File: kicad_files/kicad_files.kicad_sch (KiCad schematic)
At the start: 0 parts

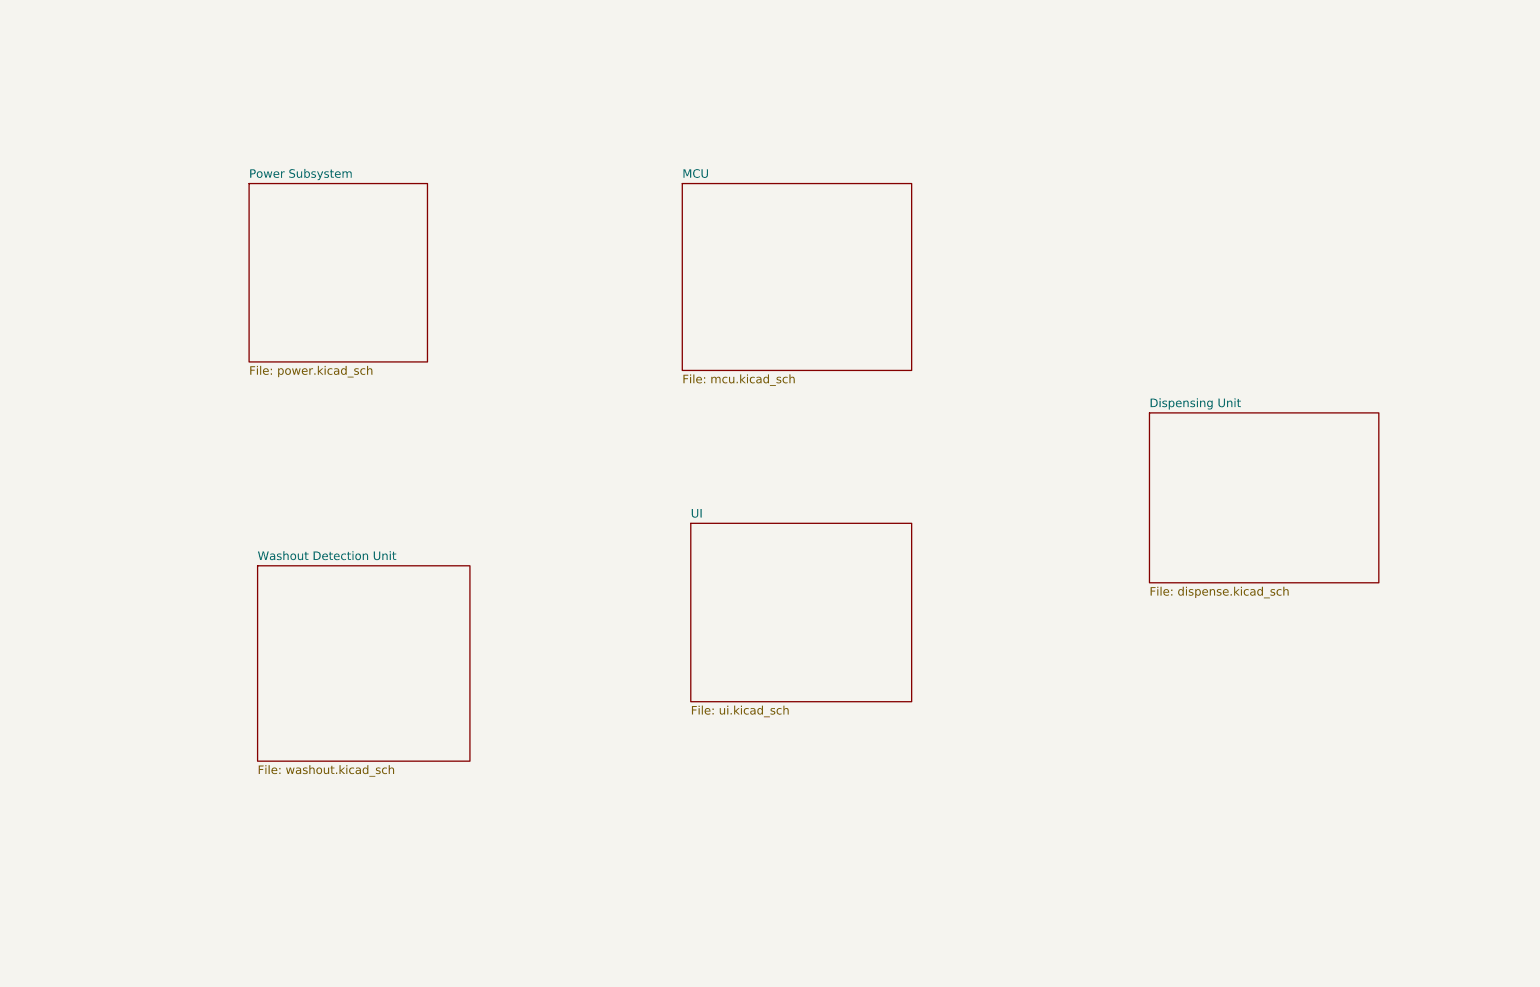
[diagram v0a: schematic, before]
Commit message: UI schematic and external connectors
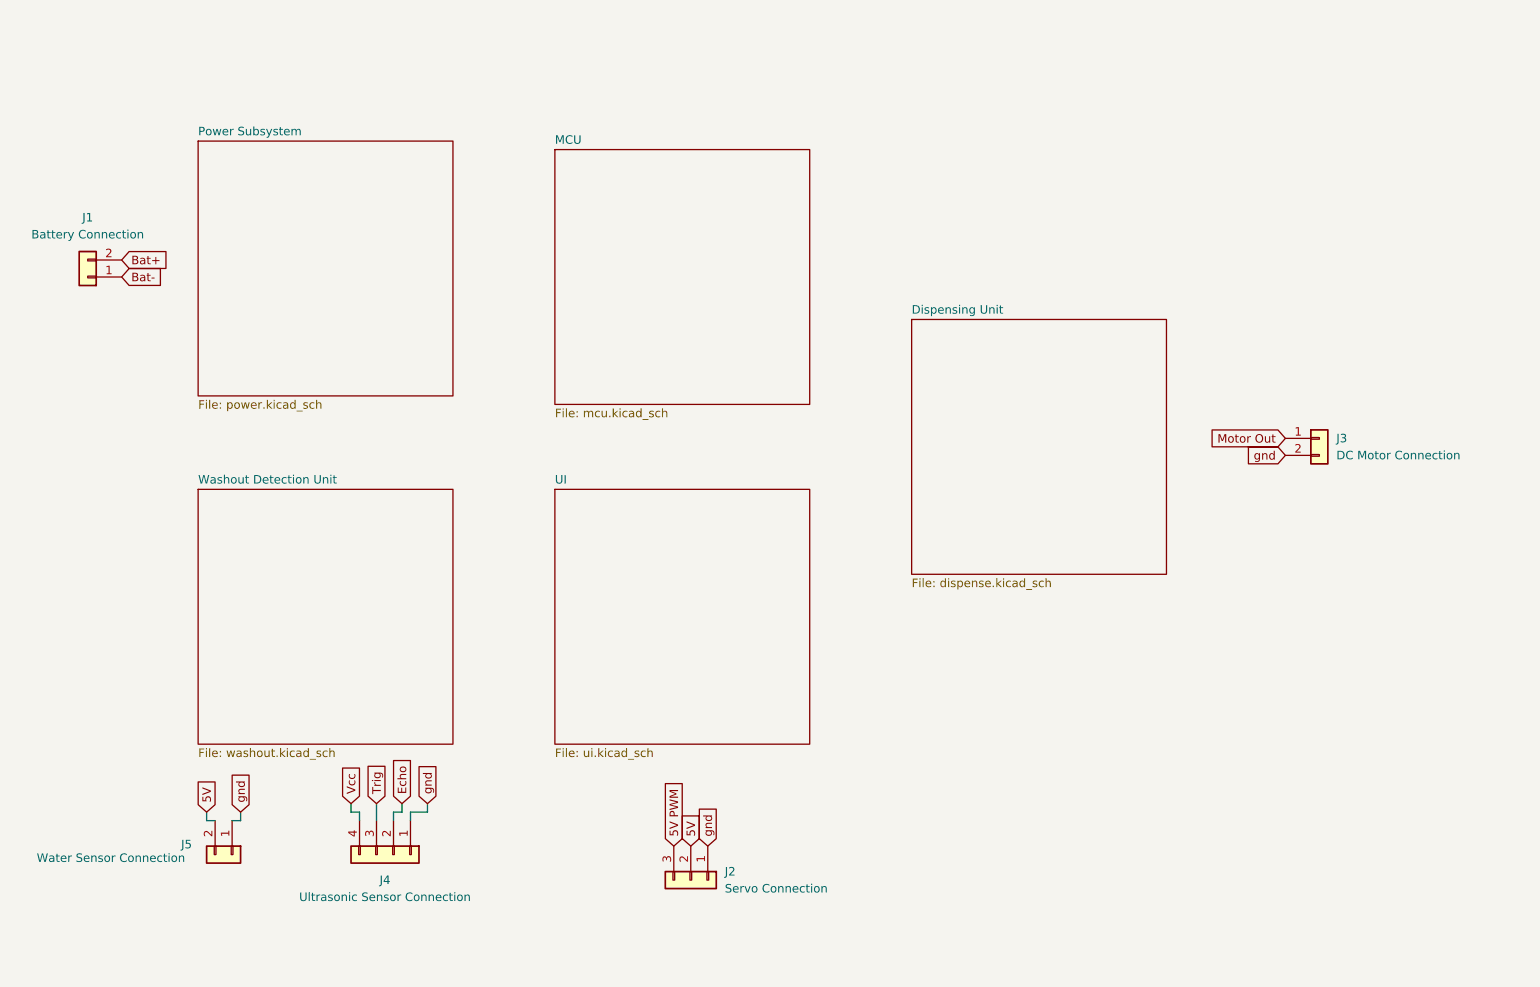
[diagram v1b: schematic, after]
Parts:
- added J1: Battery Connection, symbol Connector_Generic:Conn_01x02
- added J2: Servo Connection, symbol Connector_Generic:Conn_01x03
- added J3: DC Motor Connection, symbol Connector_Generic:Conn_01x02
- added J4: Ultrasonic Sensor Connection, symbol Connector_Generic:Conn_01x04
- added J5: Water Sensor Connection, symbol Connector_Generic:Conn_01x02
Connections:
- new net 5V: J2.2 (Pin_2), J5.2 (Pin_2)
- new net 5V PWM: J2.3 (Pin_3)
- new net Bat+: J1.2 (Pin_2)
- new net Bat-: J1.1 (Pin_1)
- new net Echo: J4.2 (Pin_2)
- new net Motor Out: J3.1 (Pin_1)
- new net Trig: J4.3 (Pin_3)
- new net Vcc: J4.4 (Pin_4)
- new net gnd: J2.1 (Pin_1), J3.2 (Pin_2), J4.1 (Pin_1), J5.1 (Pin_1)

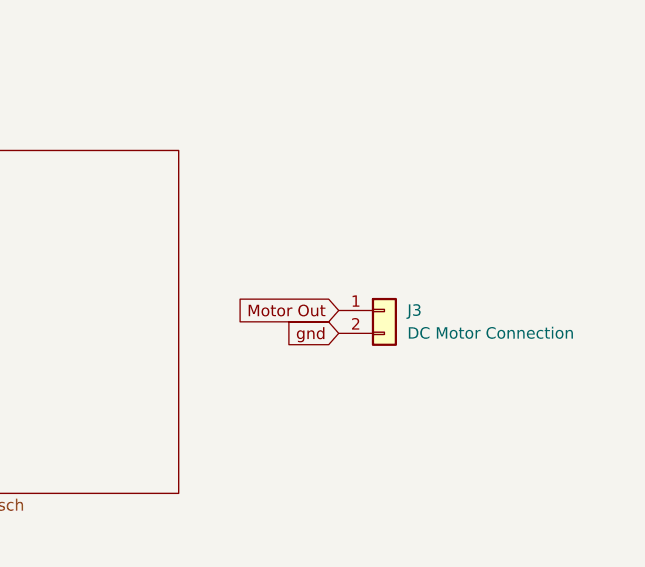
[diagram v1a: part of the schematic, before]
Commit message: UI, washout detection, motor schematics finished
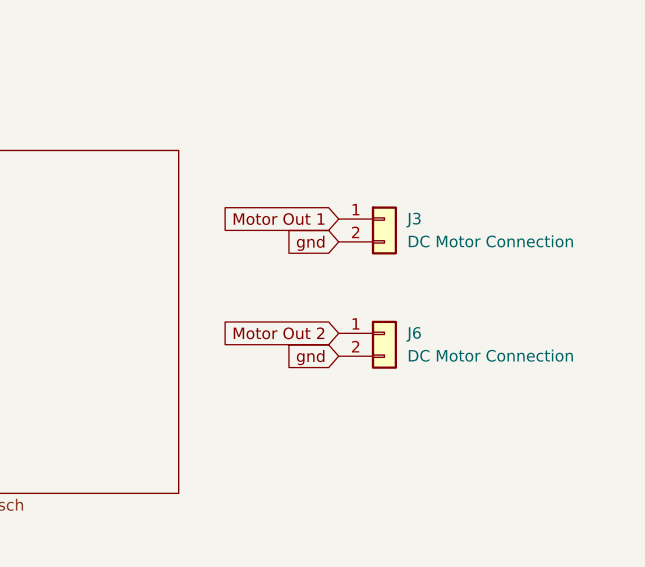
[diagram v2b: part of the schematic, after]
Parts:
- added J6: DC Motor Connection, symbol Connector_Generic:Conn_01x02
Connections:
- net gnd: now also J6.2 (Pin_2)
- net Motor Out renamed Motor Out 1
- new net Motor Out 2: J6.1 (Pin_1)
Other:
- moved on the sheet: J3
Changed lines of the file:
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@@
+		)
+	)
+	(global_label "Motor Out 2"
+		(shape input)
+		(at 207.01 110.49 180)
+		(fields_autoplaced yes)
+		(effects
+			(font
+				(size 1.27 1.27)
+			)
+			(justify right)
+		)
+		(property "Intersheetrefs" "${INTERSHEET_REFS}"
+			(at 192.4136 110.49 0)
+			(effects
+				(font
+					(size 1.27 1.27)
+				)
+				(justify right)
+				(hide yes)
+			)
 		)
 	)
@@
 		)
 	)
+	(global_label "gnd"
+		(shape input)
+		(at 207.01 113.03 180)
+		(fields_autoplaced yes)
+		(effects
+			(font
+				(size 1.27 1.27)
+			)
+			(justify right)
+		)
+		(property "Intersheetrefs" "${INTERSHEET_REFS}"
+			(at 200.5778 113.03 0)
+			(effects
+				(font
+					(size 1.27 1.27)
+				)
+				(justify right)
+				(hide yes)
+			)
+		)
+	)
 	(global_label "Vcc"
 		(shape input)
@@
 		)
 	)
-	(global_label "Motor Out"
-		(shape input)
-		(at 207.01 107.95 180)
+	(global_label "Motor Out 1"
+		(shape input)
+		(at 207.01 97.79 180)
 		(fields_autoplaced yes)
 		(effects
@@
 		)
 		(property "Intersheetrefs" "${INTERSHEET_REFS}"
-			(at 194.5907 107.95 0)
+			(at 192.4136 97.79 0)
 			(effects
 				(font
@@
 	(global_label "gnd"
 		(shape input)
-		(at 207.01 110.49 180)
+		(at 207.01 100.33 180)
 		(fields_autoplaced yes)
 		(effects
@@
 		)
 		(property "Intersheetrefs" "${INTERSHEET_REFS}"
-			(at 200.5778 110.49 0)
+			(at 200.5778 100.33 0)
 			(effects
 				(font
@@
 	(symbol
 		(lib_id "Connector_Generic:Conn_01x02")
-		(at 212.09 107.95 0)
+		(at 212.09 110.49 0)
 		(unit 1)
 		(exclude_from_sim no)
@@
 		(dnp no)
 		(fields_autoplaced yes)
+		(property "Reference" "J6"
+			(at 214.63 110.4899 0)
+			(effects
+				(font
+					(size 1.27 1.27)
+				)
+				(justify left)
+			)
+		)
+		(property "Value" "DC Motor Connection"
+			(at 214.63 113.0299 0)
+			(effects
+				(font
+					(size 1.27 1.27)
+				)
+				(justify left)
+			)
+		)
+		(property "Footprint" ""
+			(at 212.09 110.49 0)
+			(effects
+				(font
+					(size 1.27 1.27)
+				)
+				(hide yes)
+			)
+		)
+		(property "Datasheet" "~"
+			(at 212.09 110.49 0)
+			(effects
+				(font
+					(size 1.27 1.27)
+				)
+				(hide yes)
+			)
+		)
+		(property "Description" "Generic connector, single row, 01x02, script generated (kicad-library-utils/schlib/autogen/connector/)"
+			(at 212.09 110.49 0)
+			(effects
+				(font
+					(size 1.27 1.27)
+				)
+				(hide yes)
+			)
+		)
+		(pin "2"
+		)
+		(pin "1"
+		)
+		(instances
+			(project "kicad_files"
+				(path "/67de3bec-6c8a-4e66-9cf7-9a8a92865209"
+					(reference "J6")
+					(unit 1)
+				)
+			)
+		)
+	)
+	(symbol
+		(lib_id "Connector_Generic:Conn_01x02")
+		(at 212.09 97.79 0)
+		(unit 1)
+		(exclude_from_sim no)
+		(in_bom yes)
+		(on_board yes)
+		(dnp no)
+		(fields_autoplaced yes)
 		(property "Reference" "J3"
-			(at 214.63 107.9499 0)
+			(at 214.63 97.7899 0)
 			(effects
 				(font
@@
 		)
 		(property "Value" "DC Motor Connection"
-			(at 214.63 110.4899 0)
+			(at 214.63 100.3299 0)
 			(effects
 				(font
@@
 		)
 		(property "Footprint" ""
-			(at 212.09 107.95 0)
+			(at 212.09 97.79 0)
 			(effects
 				(font
@@
 		)
 		(property "Datasheet" "~"
-			(at 212.09 107.95 0)
+			(at 212.09 97.79 0)
 			(effects
 				(font
@@
 		)
 		(property "Description" "Generic connector, single row, 01x02, script generated (kicad-library-utils/schlib/autogen/connector/)"
-			(at 212.09 107.95 0)
-			(effects
-				(font
+			(at 212.09 97.79 0)
+			(effects
+				(font

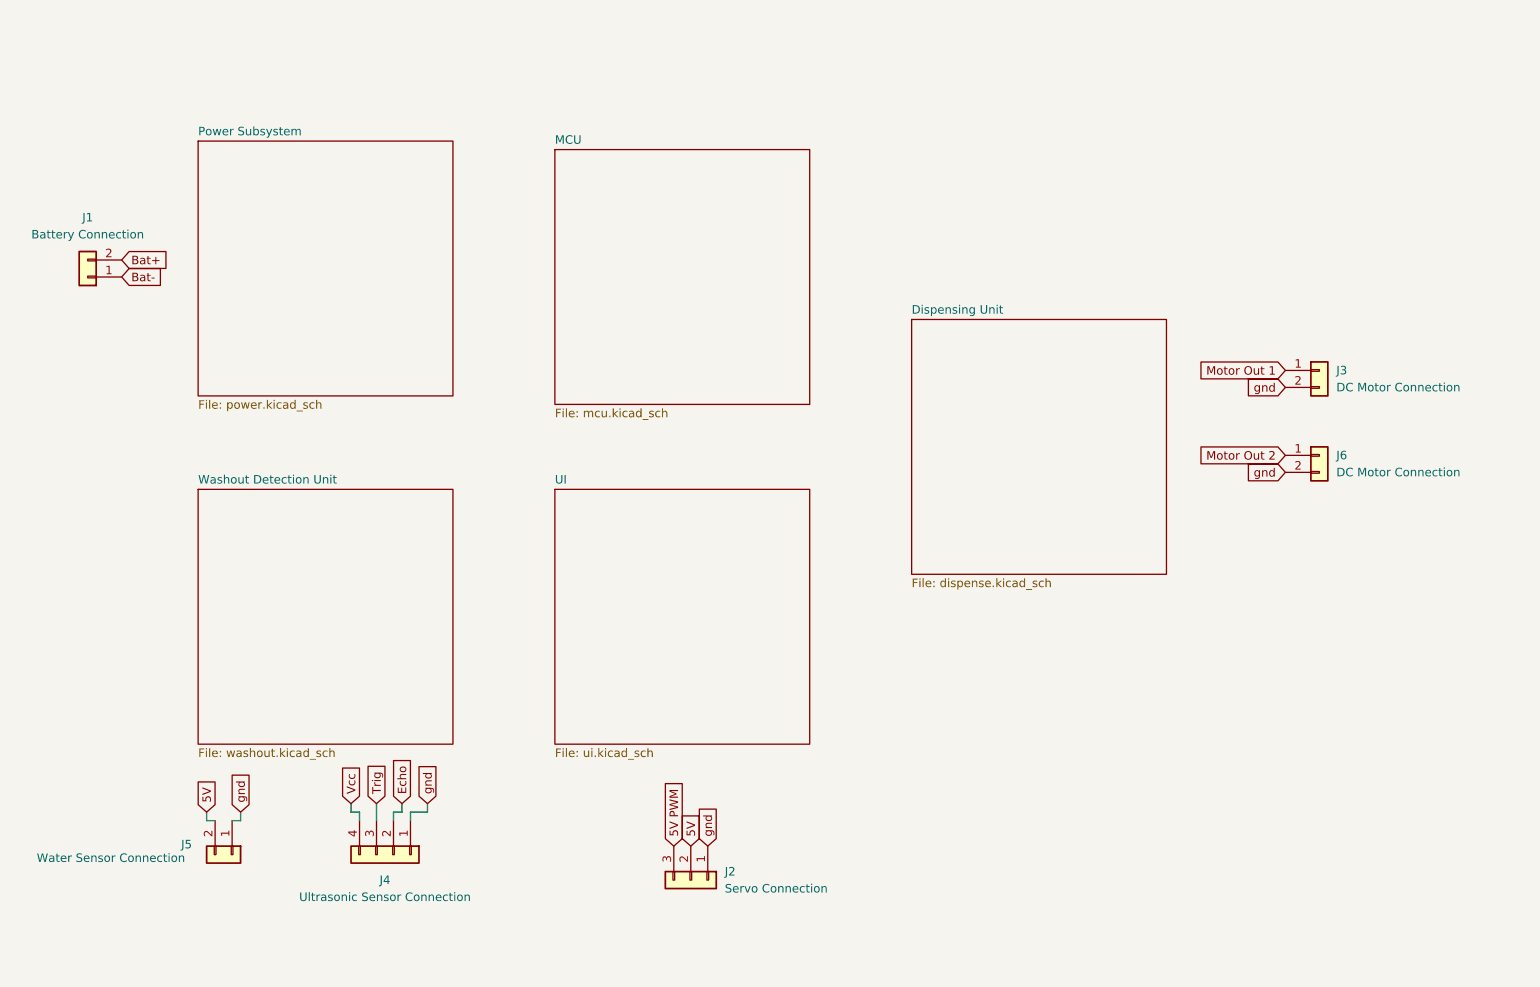
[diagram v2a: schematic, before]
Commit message: Hierarchical labels finished. Flyback diode issue fixed. I2C pins added
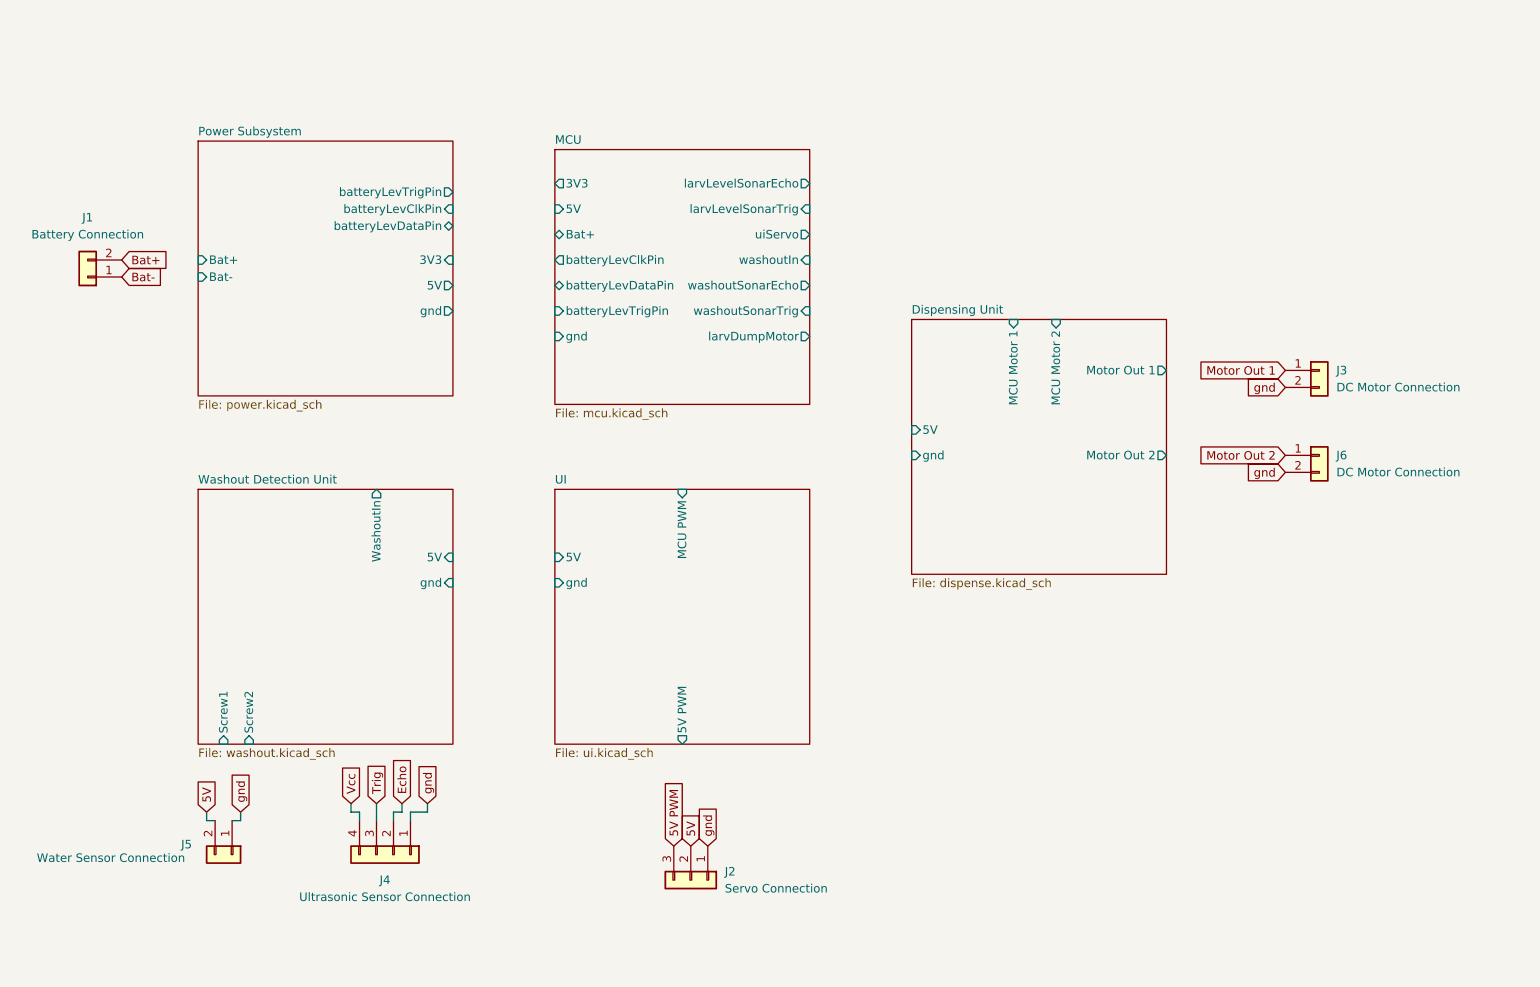
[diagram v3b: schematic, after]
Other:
- sheet Dispensing Unit ports: added 5V, MCU Motor 1, MCU Motor 2, Motor Out 1, Motor Out 2, gnd; removed none
- sheet MCU ports: added 3V3, 5V, Bat+, batteryLevClkPin, batteryLevDataPin, batteryLevTrigPin, gnd, larvDumpMotor, larvLevelSonarEcho, larvLevelSonarTrig, uiServo, washoutIn, washoutSonarEcho, washoutSonarTrig; removed none
- sheet Power Subsystem ports: added 3V3, 5V, Bat+, Bat-, batteryLevClkPin, batteryLevDataPin, batteryLevTrigPin, gnd; removed none
- sheet UI ports: added 5V, 5V PWM, MCU PWM, gnd; removed none
- sheet Washout Detection Unit ports: added 5V, Screw1, Screw2, WashoutIn, gnd; removed none
